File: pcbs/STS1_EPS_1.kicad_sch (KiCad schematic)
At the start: 4 parts, among them J1 Inter-EPS, U12 BD50GA5WEFJ

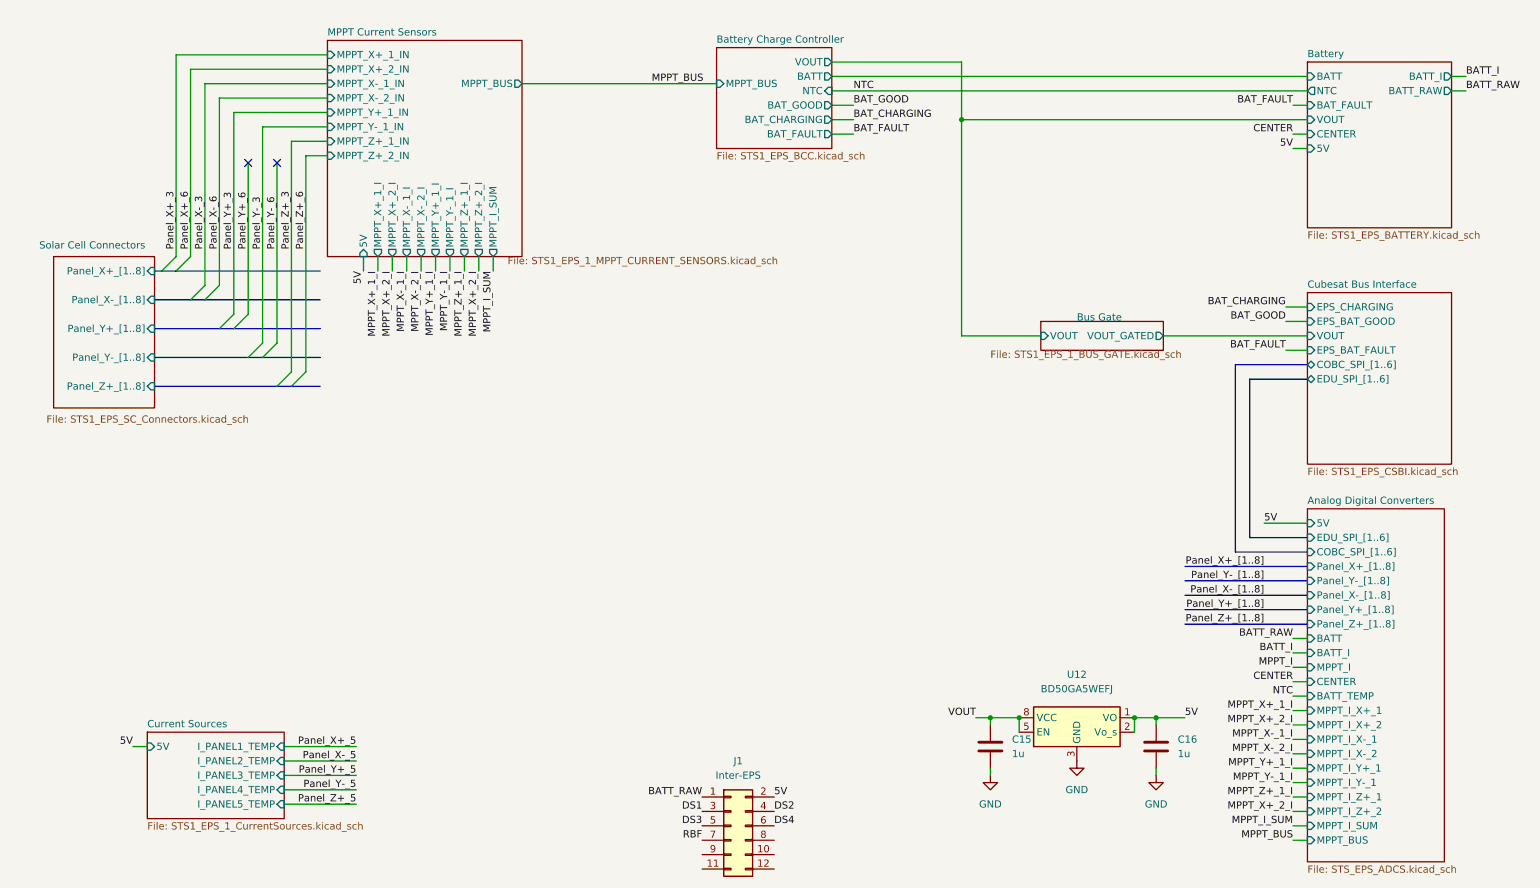
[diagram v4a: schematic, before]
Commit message: Worked on STS_EPS_1.
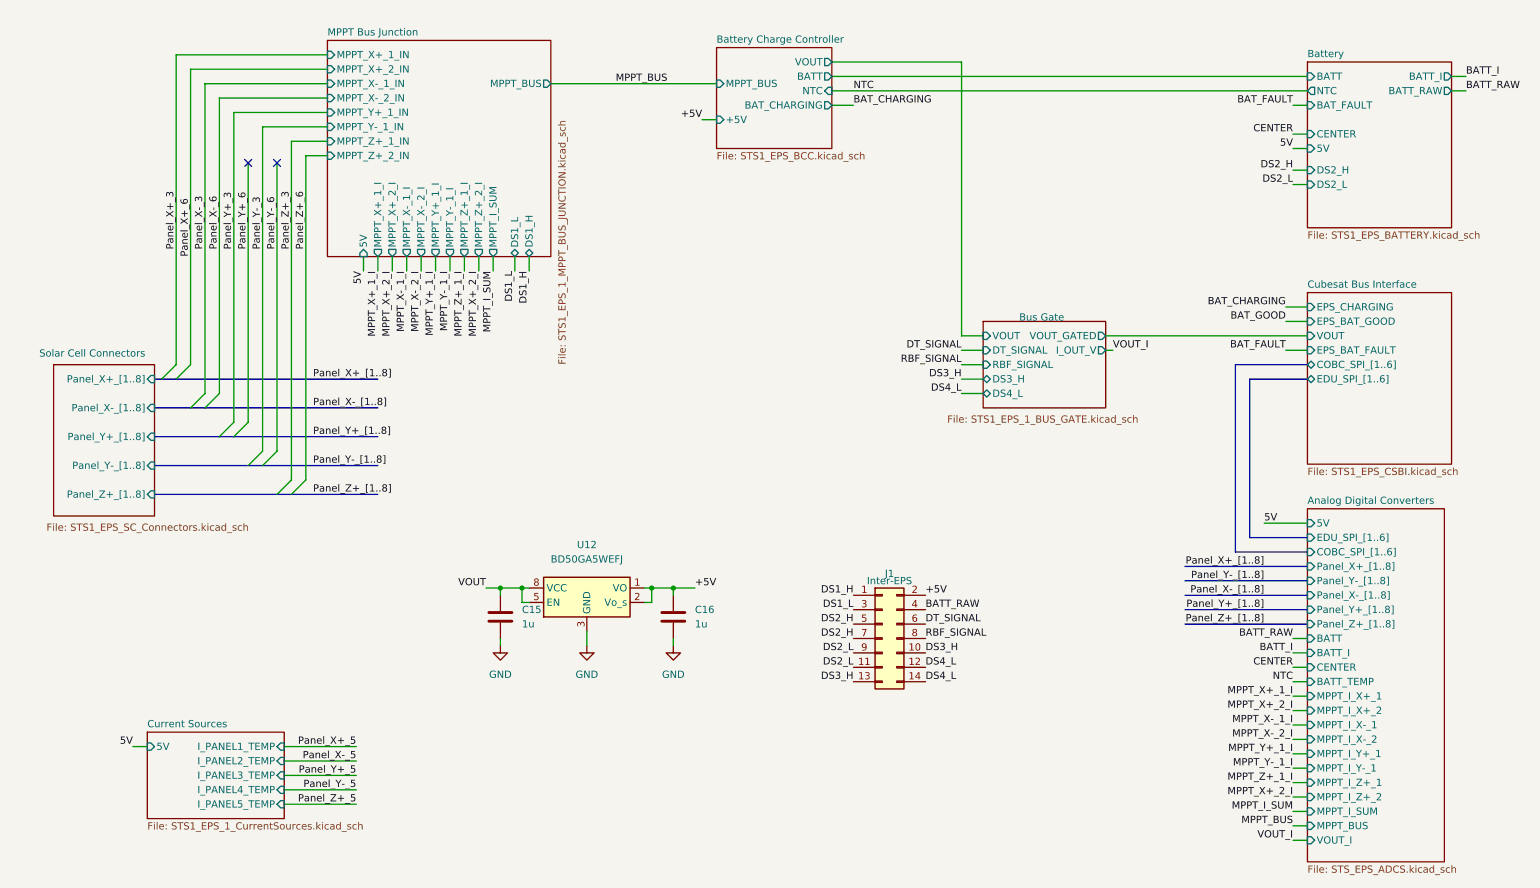
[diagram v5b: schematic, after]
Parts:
- J1: footprint (none) -> Connector_PinHeader_2.00mm:PinHeader_2x07_P2.00mm_Vertical; symbol Connector_Generic:Conn_02x06_Odd_Even -> Connector_Generic:Conn_02x07_Odd_Even
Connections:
- net DS2 is gone; now on net BATT_RAW: J1.4 (Pin_4)
- net RBF is gone; now on net DS2_H: J1.7 (Pin_7)
- net 5V: no longer C16.1, J1.2 (Pin_2), U12.1 (VO), U12.2 (Vo_s)
- net BATT_RAW: no longer J1.1 (Pin_1)
- net DS3_H: now reaches J1.10 (Pin_10)
- net DS3_H: now also J1.13 (Pin_13)
- net DS2_L: now reaches J1.11 (Pin_11)
- net DS2_L: now also J1.9 (Pin_9)
- net DS4_L: now reaches J1.12 (Pin_12)
- net DS4_L: now also J1.14 (Pin_14)
- net RBF_SIGNAL: now reaches J1.8 (Pin_8)
- net DS1 renamed DS1_L
- net DS3 renamed DS2_H
- net DS4 renamed DT_SIGNAL
- new net +5V: C16.1, J1.2 (Pin_2), U12.1 (VO), U12.2 (Vo_s)
- new net DS1_H: J1.1 (Pin_1)
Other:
- sheet MPPT Current Sensors renamed MPPT Bus Junction
- sheet Analog Digital Converters ports: added VOUT_I; removed MPPT_I
- sheet Battery ports: added DS2_H, DS2_L; removed VOUT
- sheet Battery Charge Controller ports: added +5V; removed BAT_FAULT, BAT_GOOD
- sheet Bus Gate ports: added DS3_H, DS4_L, DT_SIGNAL, I_OUT_V, RBF_SIGNAL; removed none
- sheet MPPT Bus Junction: file STS1_EPS_1_MPPT_CURRENT_SENSORS.kicad_sch -> STS1_EPS_1_MPPT_BUS_JUNCTION.kicad_sch
- sheet MPPT Bus Junction ports: added DS1_H, DS1_L; removed none
- moved on the sheet: C15, C16, U12

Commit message: Worked on STS1_EPS_1 and began work on STS1_EPS_2.
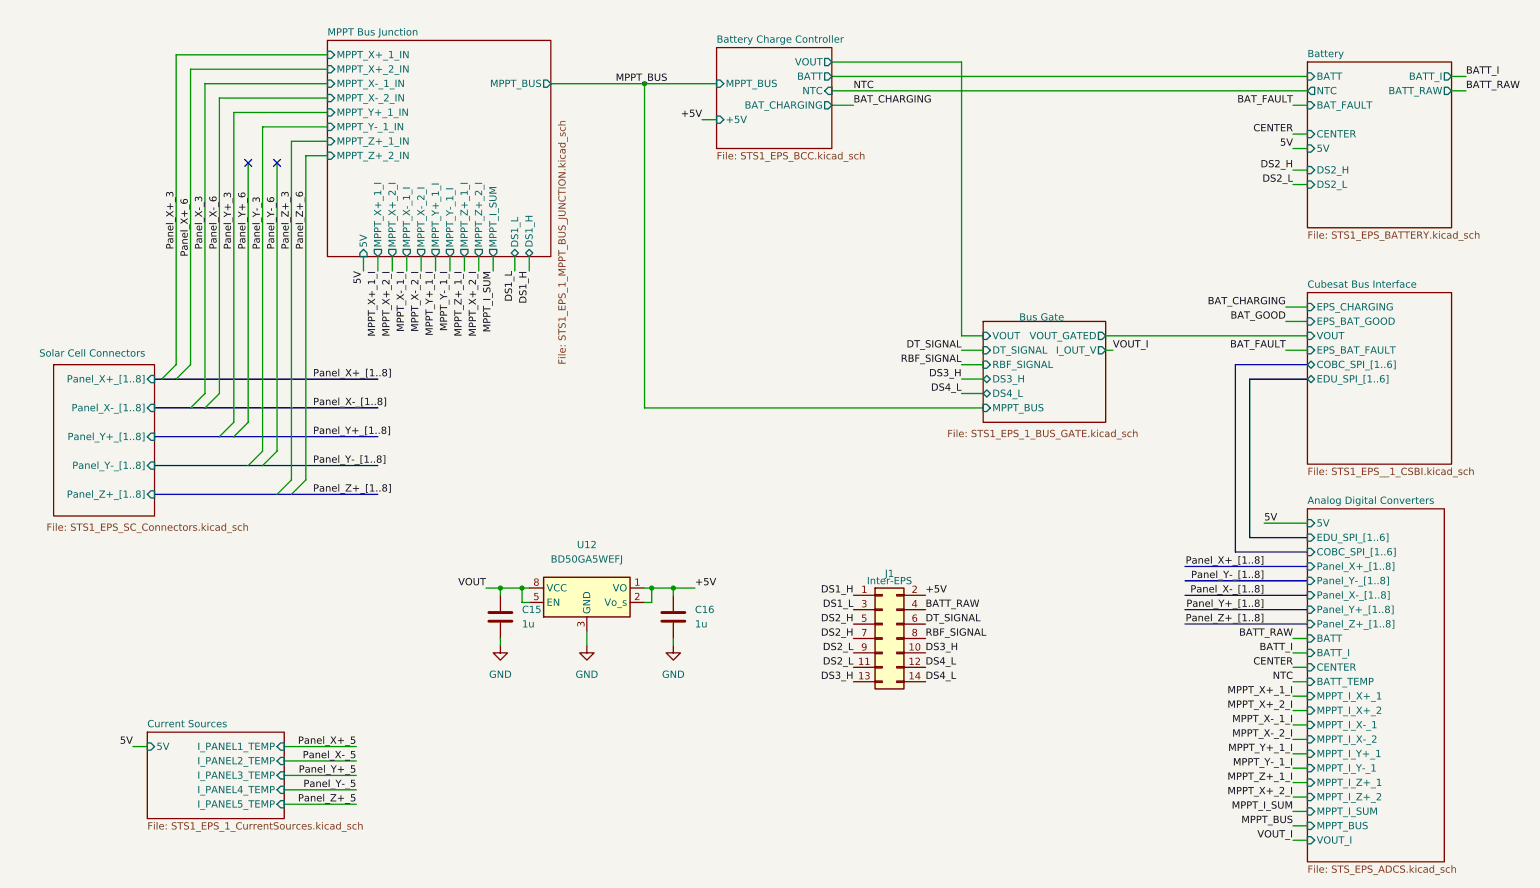
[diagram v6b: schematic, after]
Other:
- sheet Bus Gate ports: added MPPT_BUS; removed none
- sheet Cubesat Bus Interface: file STS1_EPS_CSBI.kicad_sch -> STS1_EPS__1_CSBI.kicad_sch
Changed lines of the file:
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@@
   (junction (at 92.71 114.3) (diameter 0) (color 0 0 0 0)
+  )
+  (junction (at 118.11 25.4) (diameter 0) (color 0 0 0 0)
   )
   (junction (at 96.52 114.3) (diameter 0) (color 0 0 0 0)
@@
     (stroke (width 0) (type default) (color 0 0 0 0))
   )
+  (wire (pts (xy 118.11 82.55) (xy 177.8 82.55))
+    (stroke (width 0) (type default) (color 0 0 0 0))
+  )
   (wire (pts (xy 43.18 27.94) (xy 62.23 27.94))
     (stroke (width 0) (type default) (color 0 0 0 0))
@@
     (stroke (width 0) (type default) (color 0 0 0 0))
   )
+  (wire (pts (xy 118.11 25.4) (xy 118.11 82.55))
+    (stroke (width 0) (type default) (color 0 0 0 0))
+  )
   (bus (pts (xy 38.1 82.55) (xy 40.64 82.55))
     (stroke (width 0) (type default) (color 0 0 0 0))
@@
     (stroke (width 0) (type default) (color 0 0 0 0))
   )
-  (wire (pts (xy 101.6 25.4) (xy 130.81 25.4))
+  (wire (pts (xy 101.6 25.4) (xy 118.11 25.4))
     (stroke (width 0) (type default) (color 0 0 0 0))
   )
@@
   )
   (wire (pts (xy 76.2 55.88) (xy 76.2 58.42))
+    (stroke (width 0) (type default) (color 0 0 0 0))
+  )
+  (wire (pts (xy 118.11 25.4) (xy 130.81 25.4))
     (stroke (width 0) (type default) (color 0 0 0 0))
   )
@@
       (effects (font (size 1.27 1.27)) (justify left bottom))
     )
-    (property "Sheet file" "STS1_EPS_CSBI.kicad_sch" (id 1) (at 234.95 93.0406 0)
+    (property "Sheet file" "STS1_EPS__1_CSBI.kicad_sch" (id 1) (at 234.95 93.0406 0)
       (effects (font (size 1.27 1.27)) (justify left top))
     )
@@
     )
   )
-  (sheet (at 177.8 67.31) (size 21.59 15.24)
+  (sheet (at 177.8 67.31) (size 21.59 17.78)
     (stroke (width 0.1524) (type solid) (color 0 0 0 0))
     (fill (color 255 255 0 1.0000))
@@
       (effects (font (size 1.27 1.27)) (justify left bottom))
     )
-    (property "Sheet file" "STS1_EPS_1_BUS_GATE.kicad_sch" (id 1) (at 171.45 83.82 0)
+    (property "Sheet file" "STS1_EPS_1_BUS_GATE.kicad_sch" (id 1) (at 171.45 86.36 0)
       (effects (font (size 1.27 1.27)) (justify left top))
     )
@@
     )
     (pin "DS3_H" bidirectional (at 177.8 77.47 180)
+      (effects (font (size 1.27 1.27)) (justify left))
+    )
+    (pin "MPPT_BUS" input (at 177.8 82.55 180)
       (effects (font (size 1.27 1.27)) (justify left))
     )
@@
       (reference "#PWR093") (unit 1) (value "GND") (footprint "")
     )
+    (path "/e2064052-5fd5-4fd9-90d4-ce7b28c75b19/9e7f5c17-5077-471e-9cff-677ea202c3c1"
+      (reference "#PWR094") (unit 1) (value "GND") (footprint "")
+    )
+    (path "/e2064052-5fd5-4fd9-90d4-ce7b28c75b19/ab4e8d3d-ebe1-489f-a869-2f0aacd36162"
+      (reference "#PWR095") (unit 1) (value "GND") (footprint "")
+    )
+    (path "/e2064052-5fd5-4fd9-90d4-ce7b28c75b19/4aed2e18-4063-4e0b-bc80-17ac9f9b848d"
+      (reference "#PWR096") (unit 1) (value "GND") (footprint "")
+    )
+    (path "/e2064052-5fd5-4fd9-90d4-ce7b28c75b19/fbcf7852-b06c-4cf0-bbf0-bc5aa599a928"
+      (reference "#PWR097") (unit 1) (value "GND") (footprint "")
+    )
+    (path "/e2064052-5fd5-4fd9-90d4-ce7b28c75b19/b64a8a08-fff5-4412-bea2-36257ea1fd65"
+      (reference "#PWR098") (unit 1) (value "GND") (footprint "")
+    )
+    (path "/e2064052-5fd5-4fd9-90d4-ce7b28c75b19/ca3247af-ec01-45df-b259-0c6467a979c9"
+      (reference "#PWR099") (unit 1) (value "GND") (footprint "")
+    )
+    (path "/e2064052-5fd5-4fd9-90d4-ce7b28c75b19/d992ef2c-5347-42e4-8429-ec24c6233f14"
+      (reference "#PWR0100") (unit 1) (value "GND") (footprint "")
+    )
     (path "/1fa7f756-57e9-4cd3-900e-1a1c84a07cba/6482bd63-53da-4999-b022-1368d9a158a9"
       (reference "#PWR0101") (unit 1) (value "GND") (footprint "")
@@
       (reference "#PWR0105") (unit 1) (value "GND") (footprint "")
     )
+    (path "/e2064052-5fd5-4fd9-90d4-ce7b28c75b19/32657242-fdf6-4aa4-b75c-144293c91a79"
+      (reference "#PWR0106") (unit 1) (value "GND") (footprint "")
+    )
     (path "/3f2412fd-ceb3-4d5f-b693-7628adb9c64f/aca05398-1342-4a8f-a4cd-d711c1a7ba9b"
       (reference "C1") (unit 1) (value "50u") (footprint "Capacitor_Tantalum_SMD:CP_EIA-3528-12_Kemet-T")
@@
     )
     (path "/3f2412fd-ceb3-4d5f-b693-7628adb9c64f/2ecf8c27-5a06-4677-a78b-6c66446641af"
-      (reference "C4") (unit 1) (value "680u") (footprint "")
+      (reference "C4") (unit 1) (value "680u") (footprint "Capacitor_Tantalum_SMD:CP_EIA-7343-43_Kemet-X")
     )
     (path "/3f2412fd-ceb3-4d5f-b693-7628adb9c64f/78138a8e-6850-4e86-91d3-eb5b3ed3d001"
@@
     )
     (path "/3f2412fd-ceb3-4d5f-b693-7628adb9c64f/246d1528-42e6-4397-9e4a-5b0aeee34460"
-      (reference "C32") (unit 1) (value "680u") (footprint "")
+      (reference "C32") (unit 1) (value "680u") (footprint "Capacitor_Tantalum_SMD:CP_EIA-7343-43_Kemet-X")
     )
     (path "/3f2412fd-ceb3-4d5f-b693-7628adb9c64f/c95f2ade-1fdc-45b4-9fe9-a38d44812dba"
       (reference "C33") (unit 1) (value "100p") (footprint "Capacitor_SMD:C_0805_2012Metric")
     )
+    (path "/e2064052-5fd5-4fd9-90d4-ce7b28c75b19/85b4ac38-6cb1-41a4-8023-3c58f865869d"
+      (reference "C34") (unit 1) (value "100n") (footprint "Capacitor_SMD:C_0805_2012Metric")
+    )
+    (path "/e2064052-5fd5-4fd9-90d4-ce7b28c75b19/91f16d60-a8a5-4b39-a2c9-c7e080f307cf"
+      (reference "C35") (unit 1) (value "100n") (footprint "Capacitor_SMD:C_0805_2012Metric")
+    )
     (path "/1f2aab95-1ce2-4d7d-8e47-47ae14e38d9e/00000000-0000-0000-0000-00006179b797"
       (reference "CSBI_1") (unit 1) (value "~") (footprint "Connector_PinHeader_2.00mm:PinHeader_2x25_P2.00mm_Vertical")
@@
     )
     (path "/3f2412fd-ceb3-4d5f-b693-7628adb9c64f/1f1fdffb-ad25-4e35-b984-29299b320fef"
-      (reference "L1") (unit 1) (value "680n") (footprint "Inductor_SMD:L_10.4x10.4_H4.8")
+      (reference "L1") (unit 1) (value "100u") (footprint "Inductor_SMD:L_Vishay_IHLP-4040")
     )
     (path "/3f2412fd-ceb3-4d5f-b693-7628adb9c64f/5afc5b79-309d-4228-a56a-22709fa82172"
@@
       (reference "U27") (unit 1) (value "TPS2420RSAT") (footprint "Package_DFN_QFN:VQFN-16-1EP_3x3mm_P0.5mm_EP1.45x1.45mm_ThermalVias")
     )
-  )
+    (path "/e2064052-5fd5-4fd9-90d4-ce7b28c75b19/fff12846-eff6-4eb2-bd20-b27dd071cd9f"
+      (reference "U28") (unit 1) (value "LTC4451AV#TRMPBF") (footprint "STS_Package_DFN_QFN:AD_LQFN-16")
+    )
+    (path "/e2064052-5fd5-4fd9-90d4-ce7b28c75b19/7284aa17-b888-495f-befc-8770e00ce38e"
+      (reference "U29") (unit 1) (value "LTC4451AV#TRMPBF") (footprint "STS_Package_DFN_QFN:AD_LQFN-16")
+    )
+  )

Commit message: Finished first revision of schematic.
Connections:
- net DS1_L is gone; now on net INTERNAL_V: J1.3 (Pin_3)
- net DS4_L is gone; now on net GND: J1.12 (Pin_12), J1.14 (Pin_14)
- net DT_SIGNAL is gone; now on net BATT_RAW: J1.6 (Pin_6)
- net RBF_SIGNAL is gone; now on net VOUT_I: J1.8 (Pin_8)
- net VOUT is gone; now on net INTERNAL_V: C15.1, U12.5 (EN), U12.8 (VCC)
- net DS2_H: no longer J1.5 (Pin_5), J1.7 (Pin_7)
- net DS2_L: no longer J1.11 (Pin_11), J1.9 (Pin_9)
- net GND: now also J1.11 (Pin_11), J1.13 (Pin_13)
- net DS1_H renamed INTERNAL_V
- net INTERNAL_V: now also J1.5 (Pin_5), J1.7 (Pin_7)
- net DS3_H renamed DS2_SIGNAL_1
- net DS2_SIGNAL_1: no longer J1.13 (Pin_13)
- new net DS1_SIGNAL_1: J1.9 (Pin_9)
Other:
- removed sheet Bus Gate
- added sheet Power ORing (STS1_EPS_1_ORING.kicad_sch)
- sheet Battery Charge Controller ports: added BAT_FAULT; removed none
- sheet Cubesat Bus Interface ports: added none; removed EPS_BAT_GOOD, VOUT
- sheet MPPT Bus Junction ports: added DS1_SIGNAL, DS2_SIGNAL; removed DS1_H, DS1_L
- moved on the sheet: C15, C16, J1, U12
